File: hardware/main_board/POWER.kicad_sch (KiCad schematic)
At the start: 13 parts, among them IC4 TPS63000IDRCRQ1, J6 UJC-H-G-SMT-1-P6-TR

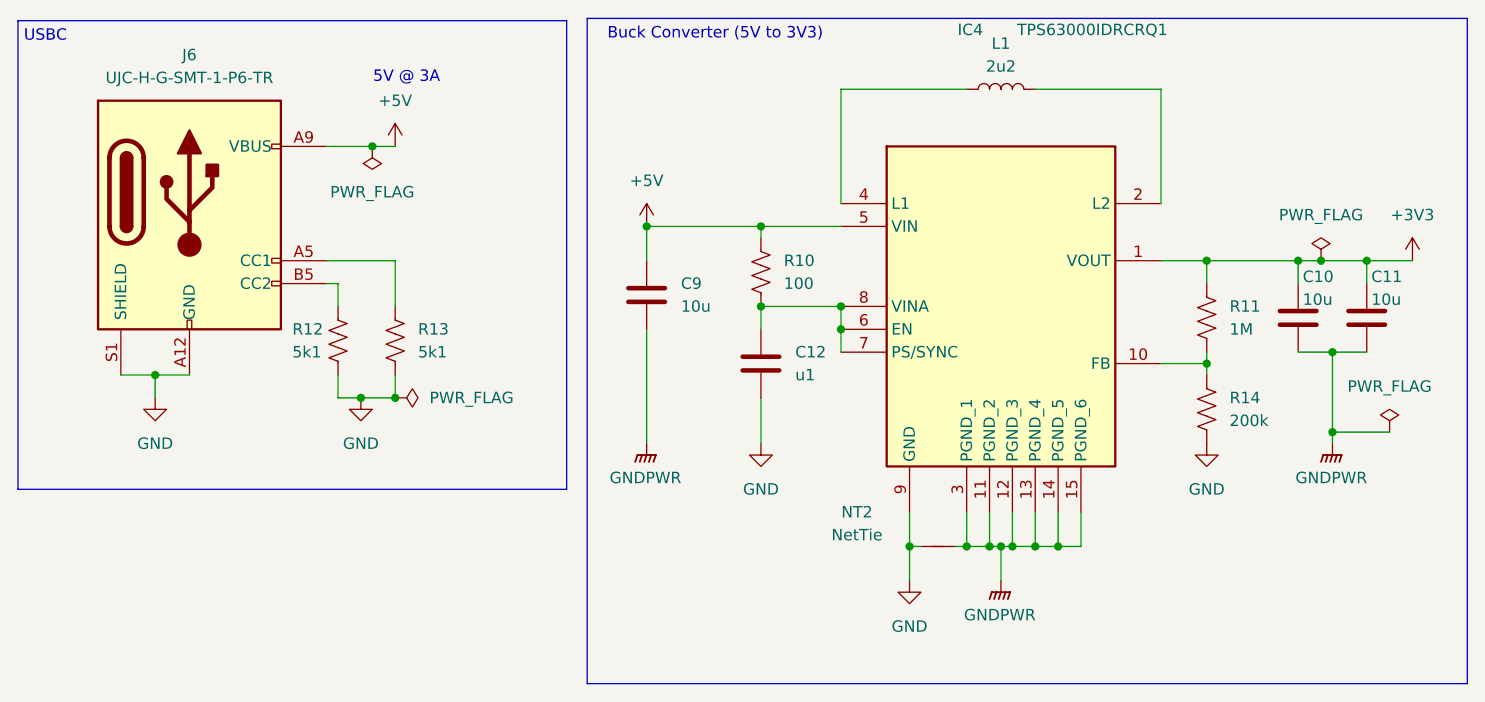
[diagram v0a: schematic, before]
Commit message: added lakshay suggestions to peripheral board. removed bypass jumper from main board audio amp. added led strip interface. added too many things to remember i forgor
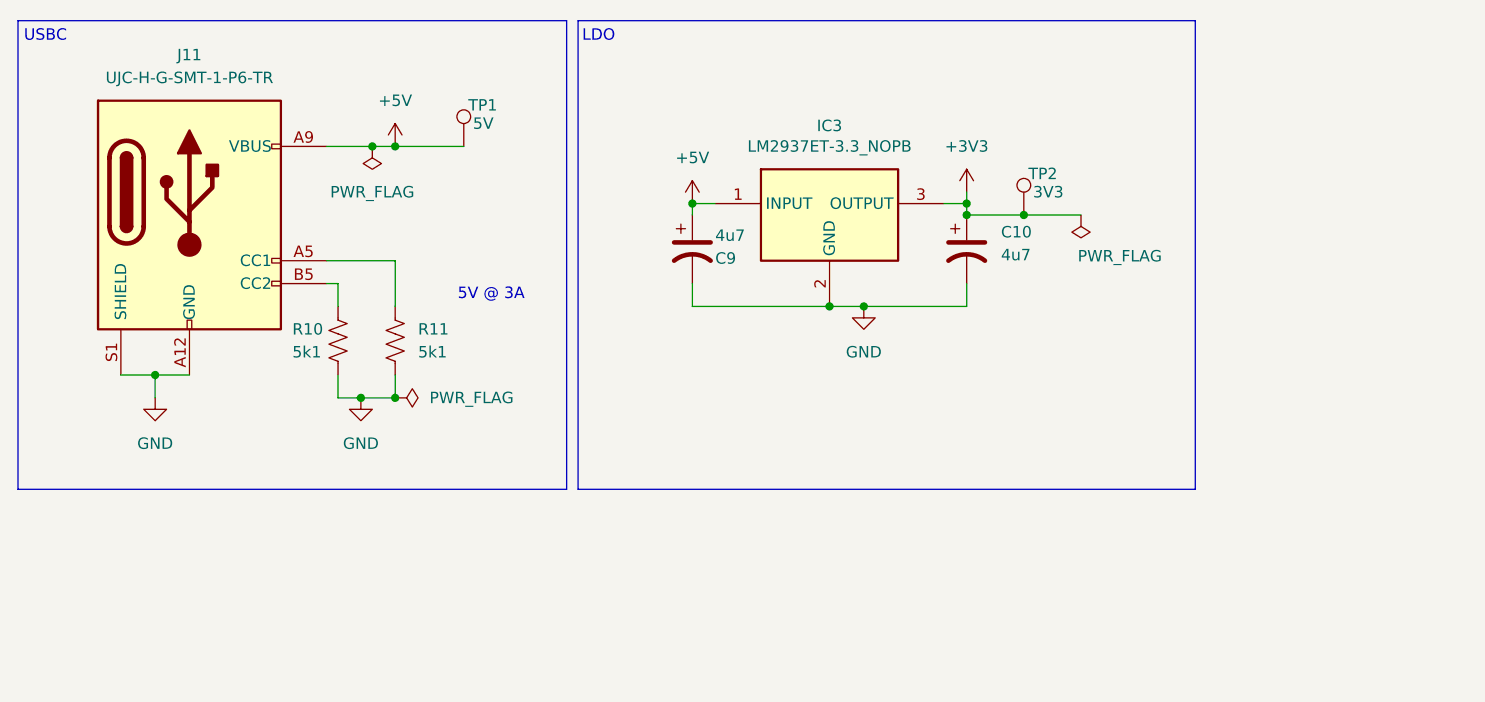
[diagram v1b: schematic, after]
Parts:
- removed C10, C11, C9: 10u, Capacitor_SMD:C_0805_2012Metric, symbol Device:C
- removed C12: u1, Capacitor_SMD:C_0805_2012Metric, symbol Device:C
- removed IC4: TPS63000IDRCRQ1, SamacSys_Parts:TPS63000IDRCRQ1, symbol SamacSys_Parts:TPS63000IDRCRQ1
- removed L1: 2u2, SamacSys_Parts:NRS3015T2R2MNGHV, symbol Device:L
- removed NT2: NetTie, NetTie:NetTie-3_SMD_Pad2.0mm, symbol SamacSys_Parts:NetTie
- removed R10: 100, Resistor_SMD:R_0805_2012Metric, symbol Device:R_US
- removed R11: 1M, Resistor_SMD:R_0805_2012Metric, symbol Device:R_US
- removed R14: 200k, Resistor_SMD:R_0805_2012Metric, symbol Device:R_US
- added C10: 4u7, 445L:CP_Radial_Tantal200mil, symbol Device:C_Polarized_US
- added C9: 4u7, 445L:CP_Radial_Tantal200mil, symbol ECE445L:C_Polarized
- added IC3: LM2937ET-3.3_NOPB, 445L:TO254P470X1028X1955-3P, symbol ECE445L:LM2937ET-3.3_NOPB
- added TP1: 5V, SamacSys_Parts:bettertestpoint2, symbol Connector:TestPoint
- added TP2: 3V3, SamacSys_Parts:bettertestpoint2, symbol Connector:TestPoint
- renumbered J6 to J11, R12 to R10, R13 to R11
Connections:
- net +3V3: now also C10.1, IC3.3 (OUTPUT), TP2.1
- net +5V: now also C9.1, IC3.1 (INPUT), TP1.1
- net GND: now also C10.2, C9.2, IC3.2 (GND)
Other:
- note added: "LDO"
- note removed: "Buck Converter (5V to 3V3)"
